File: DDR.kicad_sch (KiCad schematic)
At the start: 1 part, among them U2 rv1126/rv1109

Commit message: PMIC DCDC
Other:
- title: Leaf RV1126 Power -> Leaf RV1126 PMIC RK809
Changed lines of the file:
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@@
   (paper "A4")
   (title_block
-    (title "Leaf RV1126 Power")
+    (title "Leaf RV1126 PMIC RK809")
     (date "2023-02-23")
     (rev "1")

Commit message: updated: PMIC codec
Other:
- title: Leaf RV1126 PMIC RK809 -> Leaf RV1126 PMIC RK809 Codec
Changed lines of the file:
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@@
   (paper "A4")
   (title_block
-    (title "Leaf RV1126 PMIC RK809")
-    (date "2023-02-23")
+    (title "Leaf RV1126 PMIC RK809 Codec")
+    (date "2023-02-25")
     (rev "1")
     (company "Qingdao IotPi Information Technology")

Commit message: updated: titles
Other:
- title: Leaf RV1126 PMIC RK809 Codec -> Leaf RV1126 RK809 DDR
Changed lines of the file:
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@@
   (paper "A4")
   (title_block
-    (title "Leaf RV1126 PMIC RK809 Codec")
+    (title "Leaf RV1126 RK809 DDR")
     (date "2023-02-25")
     (rev "1")

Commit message: updated: DDR
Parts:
- added U4: W634GU6QB, Package_BGA:Micron_FBGA-96_7.5x13.5mm_Layout9x16_P0.8mm, symbol Memory_DDR:W634GU6QB
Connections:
- net DDR resistors/SoC_A8: now reaches U2.A10 (LPDDR4_CLKN_A/DDR4_A10/LPDDR3_A8/DDR3_A8)
- net DDR resistors/SoC_A14: now reaches U2.A11 (LPDDR4_CS1n_B/DDR4_A14_Wen/DDR3_A14)
- net DDR resistors/SoC_A13: now reaches U2.A12 (LPDDR4_A3_A/DDR4_A13/DDR3_A13)
- net DDR resistors/SoC_CKE: now reaches U2.A4 (LPDDR4_A3_B/DDR4_ACTn/LPDDR3_CKE/DDR3_CKE)
- net DDR resistors/SoC_CS0n: now reaches U2.A5 (LPDDR4_A4_B/DDR4_ODT0/LPDDR3_CS0n/DDR3_CS0n)
- net DDR resistors/SoC_WEn: now reaches U2.A6 (LPDDR4_CKE1_B/DDR4_BA1/DDR3_WEn)
- net DDR resistors/SoC_A12: now reaches U2.A7 (LPDDR4_ODT0_B/DDR4_A5/DDR3_A12)
- net DDR resistors/SoC_A1: now reaches U2.A8 (LPDDR4_CKE0_A/DDR4_A8/LPDDR3_A1/DDR3_A1)
- net DDR resistors/SoC_A6: now reaches U2.A9 (LPDDR4_CLKP_A/DDR4_A4/LPDDR3_A6/DDR3_A6)
- net DDR resistors/SoC_A11: now reaches U2.B10 (LPDDR4_CS0n_B/DDR4_A16_RASn/DDR3_A11)
- net DDR resistors/SoC_A9: now reaches U2.B11 (LPDDR4_A4_A/DDR4_A2/LPDDR3_A9/DDR3_A9)
- net DDR resistors/SoC_ODT0: now reaches U2.B4 (LPDDR4_A2_B/DDR4_CS0n/LPDDR3_ODT0/DDR3_ODT0)
- net DDR resistors/SoC_A10: now reaches U2.B5 (LPDDR4_A0_B/DDR4_A15_CASn/DDR3_A10)
- net DDR resistors/SoC_A15: now reaches U2.B6 (LPDDR4_A5_B/DDR4_A3/DDR3_A15)
- net DDR resistors/SoC_BA1: now reaches U2.B7 (LPDDR4_CKE0_B/DDR4_A1/DDR3_BA1)
- net DDR resistors/SoC_A4: now reaches U2.B8 (LPDDR4_ODT0_A/DDR4_A7/LPDDR3_A4/DDR3_A4)
- net DDR resistors/SoC_A5: now reaches U2.B9 (LPDDR4_A5_A/DDR4_A9/LPDDR3_A5/DDR3_A5)
- net DDR resistors/SoC_A7: now reaches U2.C11 (LPDDR4_A2_A/DDR4_A11/LPDDR3_A7/DDR3_A7)
- net DDR resistors/SoC_CASn: now reaches U2.C6 (LPDDR4_A1_B/DDR4_CKE/DDR3_CASn)
- net DDR resistors/SoC_BA2: now reaches U2.C8 (LPDDR4_A0_A/DDR4_A6/DDR3_BA2)
- net DDR resistors/SoC_A3: now reaches U2.C9 (LPDDR4_CKE1_A/DDR4_A0/LPDDR3_A3/DDR3_A3)
- net DDR resistors/SoC_A0: now reaches U2.D10 (LPDDR4_ODT1_B/DDR4_ODT1/LPDDR3_A0/DDR3_A0)
- net DDR resistors/SoC_A2: now reaches U2.D11 (LPDDR4_ODT1_A/DDR4_BG1/LPDDR3_A2/DDR3_A2)
- net DDR resistors/SoC_ODT1: now reaches U2.D6 (LPDDR4_CS1n_A/DDR4_BG0/LPDDR3_ODT1/DDR3_ODT1)
- net DDR resistors/SoC_BA0: now reaches U2.D8 (DDR4_CS1n/DDR3_BA0)
- net DDR resistors/SoC_CS1n: now reaches U2.E7 (LPDDR4_CS0n_A/DDR4_BA0/LPDDR3_CS1n/DDR3_CS1n)
- new net DDR resistors/DDR_A0: U4.N3 (A0)
- new net DDR resistors/DDR_A1: U4.P7 (A1)
- new net DDR resistors/DDR_A10: U4.L7 (A10/AP)
- new net DDR resistors/DDR_A11: U4.R7 (A11)
- new net DDR resistors/DDR_A12: U4.N7 (A12/BC#)
- new net DDR resistors/DDR_A13: U4.T3 (A13)
- new net DDR resistors/DDR_A14: U4.T7 (A14)
- new net DDR resistors/DDR_A2: U4.P3 (A2)
- new net DDR resistors/DDR_A3: U4.N2 (A3)
- new net DDR resistors/DDR_A4: U4.P8 (A4)
- new net DDR resistors/DDR_A5: U4.P2 (A5)
- new net DDR resistors/DDR_A6: U4.R8 (A6)
- new net DDR resistors/DDR_A7: U4.R2 (A7)
- new net DDR resistors/DDR_A8: U4.T8 (A8)
- new net DDR resistors/DDR_A9: U4.R3 (A9)
- new net DDR resistors/DDR_BA0: U4.M2 (BA0)
- new net DDR resistors/DDR_BA1: U4.N8 (BA1)
- new net DDR resistors/DDR_BA2: U4.M3 (BA2)
- new net DDR resistors/DDR_CASn: U4.K3 (CAS#)
- new net DDR resistors/DDR_CKE: U4.K9 (CKE)
- new net DDR resistors/DDR_CS0n: U4.L2 (CS#)
- new net DDR resistors/DDR_ODT0: U4.K1 (ODT)
- new net DDR resistors/DDR_WEn: U4.L3 (WE#)
- no-connect marks 0 -> 3
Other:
- added sheet DDR resistors (DDR_resistors.kicad_sch)
- moved on the sheet: U2N

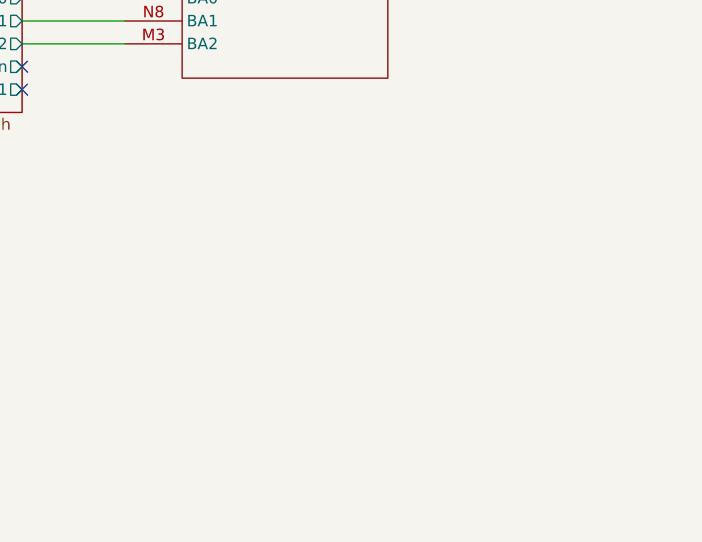
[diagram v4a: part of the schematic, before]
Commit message: added DDR Power
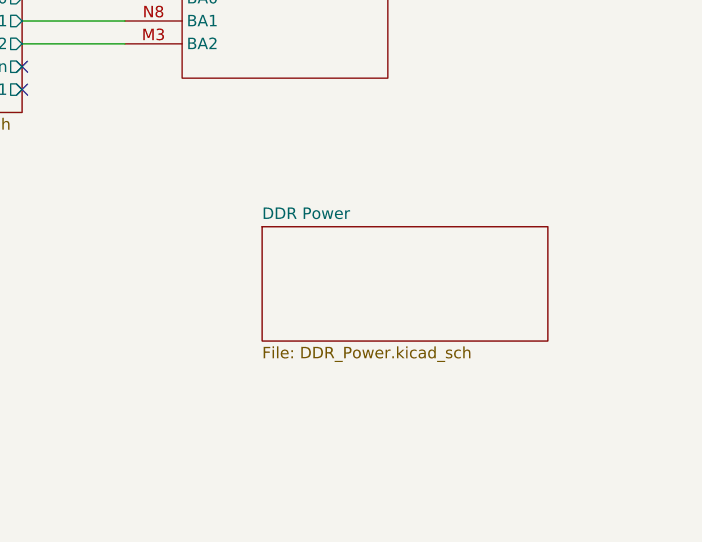
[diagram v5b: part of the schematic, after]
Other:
- added sheet DDR Power (DDR_Power.kicad_sch)
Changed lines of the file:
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@@
+    )
+  )
+  (sheet (at 232.41 127) (size 31.75 12.7) (fields_autoplaced)
+    (stroke (width 0.1524) (type solid))
+    (fill (color 0 0 0 0.0000))
+    (property "Sheetname" "DDR Power" (at 232.41 126.2884 0)
+      (effects (font (size 1.27 1.27)) (justify left bottom))
+    )
+    (property "Sheetfile" "DDR_Power.kicad_sch" (at 232.41 140.2846 0)
+      (effects (font (size 1.27 1.27)) (justify left top))
+    )
+    (instances
+      (project "leaf"
+        (path "/e3b58043-16a3-43c8-9fad-9c9784eebfa4/9453ad46-b3ff-4d4e-8aa6-7cc75aa0f522" (page "18"))
+      )
     )
   )

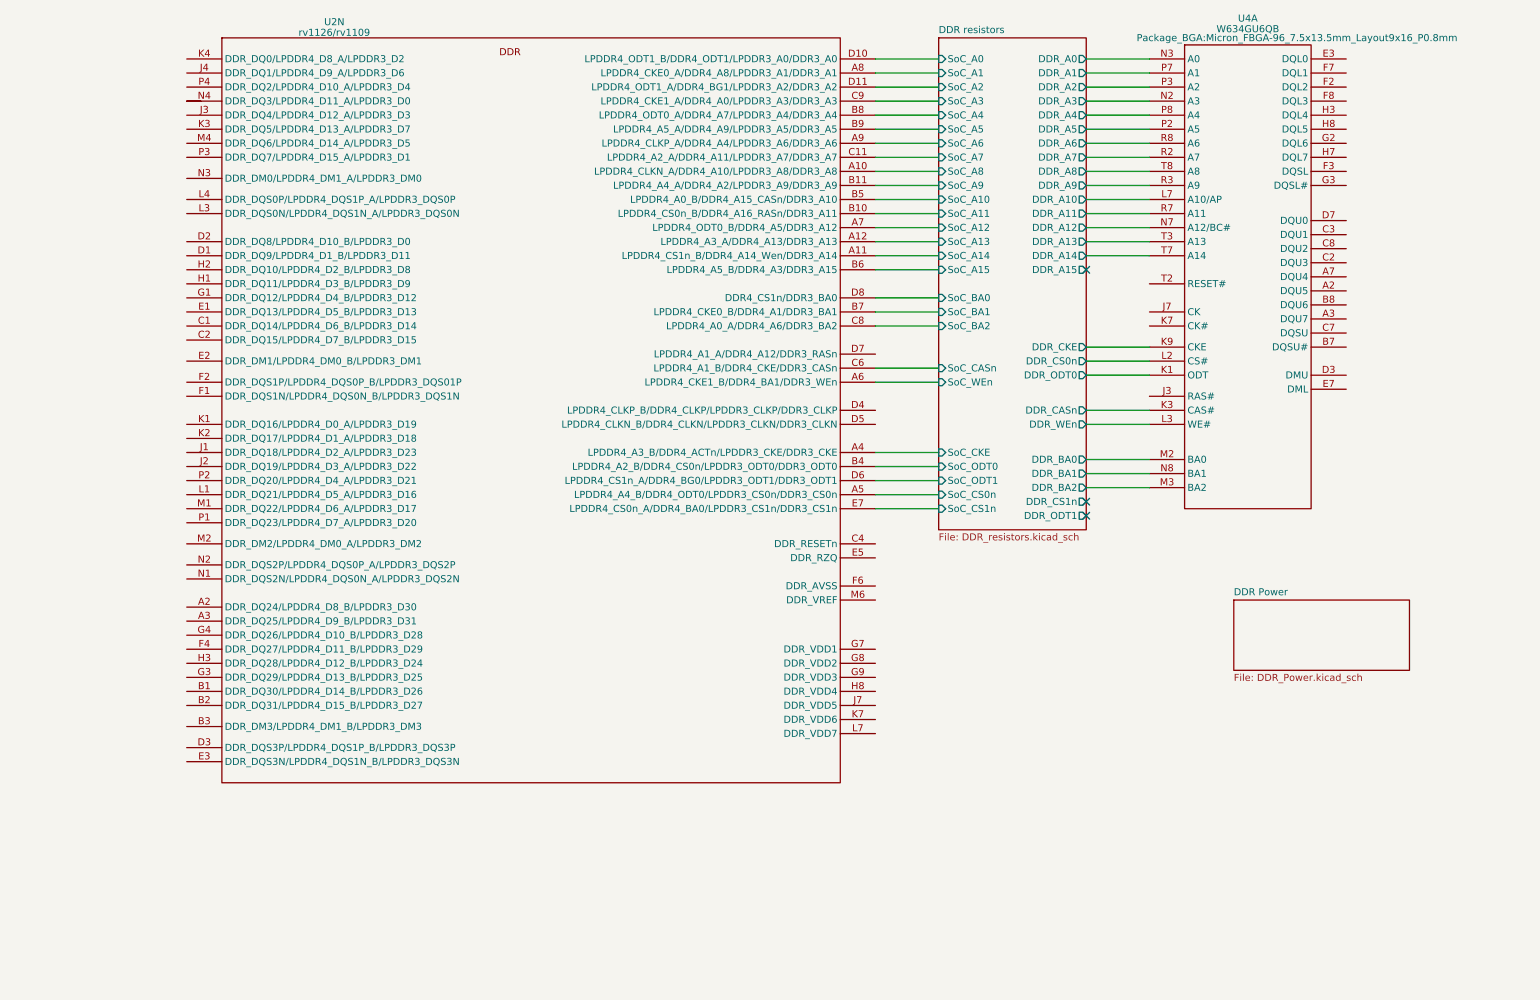
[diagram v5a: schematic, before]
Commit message: updated DDR data lines
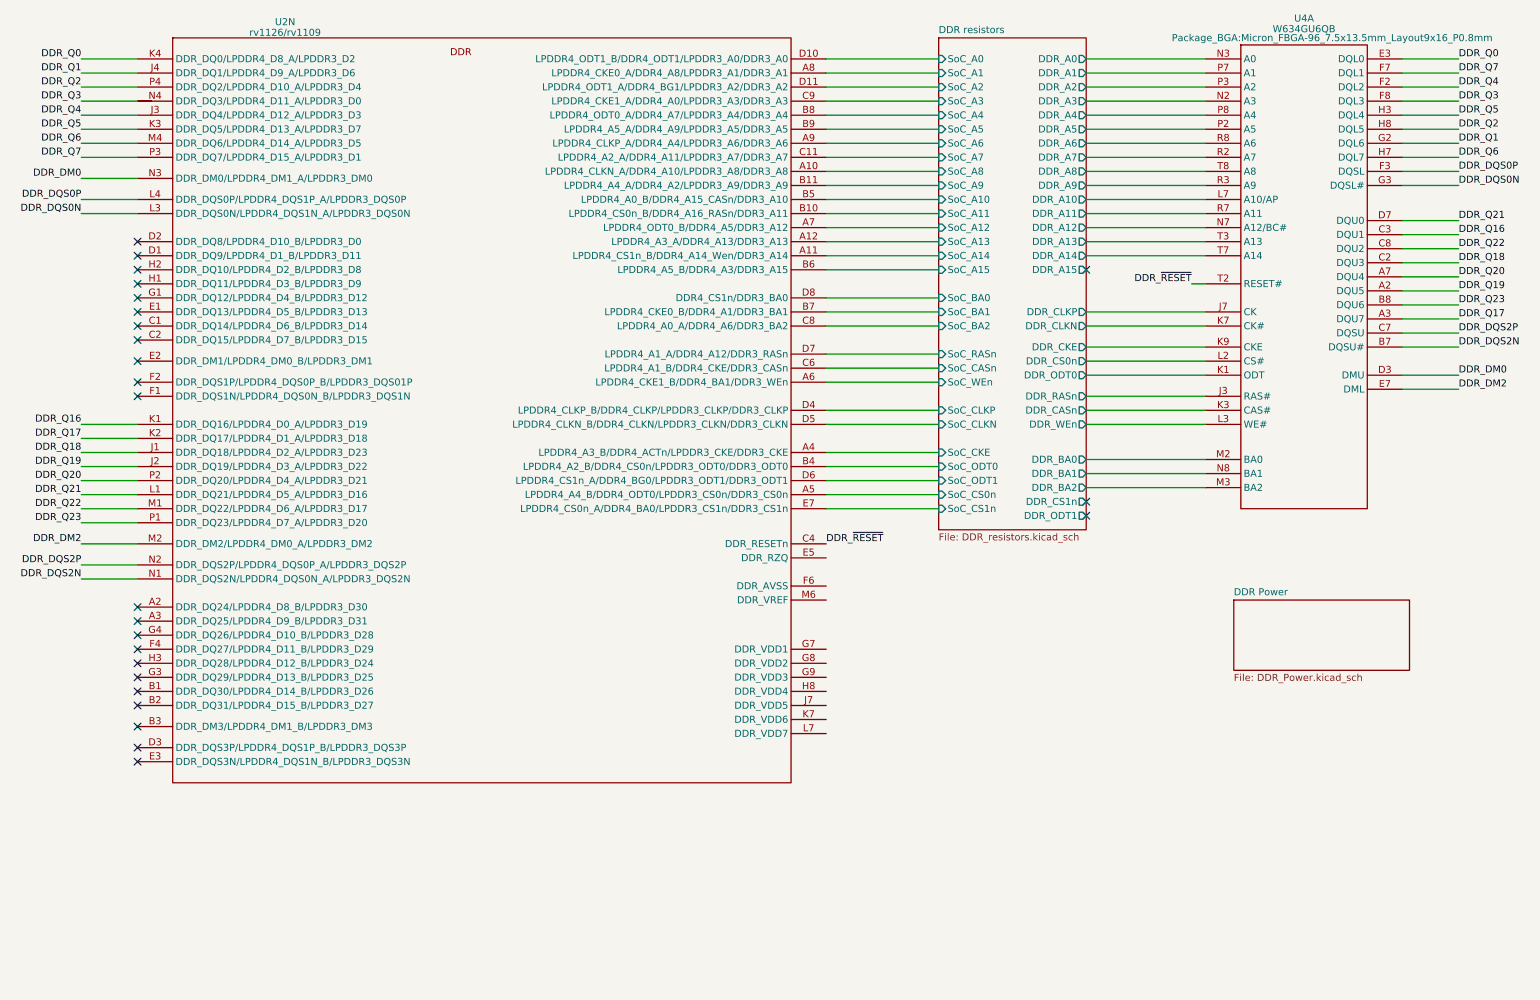
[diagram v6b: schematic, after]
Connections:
- net DDR_Q19: now reaches U4.A2 (DQU5)
- net DDR_Q19: now also U2.J2 (DDR_DQ19/LPDDR4_D3_A/LPDDR3_D22)
- net DDR_Q17: now reaches U4.A3 (DQU7)
- net DDR_Q17: now also U2.K2 (DDR_DQ17/LPDDR4_D1_A/LPDDR3_D18)
- net DDR_Q20: now reaches U4.A7 (DQU4)
- net DDR_Q20: now also U2.P2 (DDR_DQ20/LPDDR4_D4_A/LPDDR3_D21)
- net DDR_DQS2N: now reaches U4.B7 (DQSU#)
- net DDR_DQS2N: now also U2.N1 (DDR_DQS2N/LPDDR4_DQS0N_A/LPDDR3_DQS2N)
- net DDR_Q23: now reaches U4.B8 (DQU6)
- net DDR_Q23: now also U2.P1 (DDR_DQ23/LPDDR4_D7_A/LPDDR3_D20)
- net DDR_Q18: now reaches U4.C2 (DQU3)
- net DDR_Q18: now also U2.J1 (DDR_DQ18/LPDDR4_D2_A/LPDDR3_D23)
- net DDR_Q16: now reaches U4.C3 (DQU1)
- net DDR_Q16: now also U2.K1 (DDR_DQ16/LPDDR4_D0_A/LPDDR3_D19)
- net DDR_DQS2P: now reaches U4.C7 (DQSU)
- net DDR_DQS2P: now also U2.N2 (DDR_DQS2P/LPDDR4_DQS0P_A/LPDDR3_DQS2P)
- net DDR_Q22: now reaches U4.C8 (DQU2)
- net DDR_Q22: now also U2.M1 (DDR_DQ22/LPDDR4_D6_A/LPDDR3_D17)
- net DDR_DM0: now reaches U4.D3 (DMU)
- net DDR_DM0: now also U2.N3 (DDR_DM0/LPDDR4_DM1_A/LPDDR3_DM0)
- net DDR_Q21: now reaches U4.D7 (DQU0)
- net DDR_Q21: now also U2.L1 (DDR_DQ21/LPDDR4_D5_A/LPDDR3_D16)
- net DDR_Q0: now reaches U4.E3 (DQL0)
- net DDR_Q0: now also U2.K4 (DDR_DQ0/LPDDR4_D8_A/LPDDR3_D2)
- net DDR_DM2: now reaches U4.E7 (DML)
- net DDR_DM2: now also U2.M2 (DDR_DM2/LPDDR4_DM0_A/LPDDR3_DM2)
- net DDR_Q4: now reaches U4.F2 (DQL2)
- net DDR_Q4: now also U2.J3 (DDR_DQ4/LPDDR4_D12_A/LPDDR3_D3)
- net DDR_DQS0P: now reaches U4.F3 (DQSL)
- net DDR_DQS0P: now also U2.L4 (DDR_DQS0P/LPDDR4_DQS1P_A/LPDDR3_DQS0P)
- net DDR_Q7: now reaches U4.F7 (DQL1)
- net DDR_Q7: now also U2.P3 (DDR_DQ7/LPDDR4_D15_A/LPDDR3_D1)
- net DDR_Q3: now reaches U4.F8 (DQL3)
- net DDR_Q3: now also U2., U2.N4 (DDR_DQ3/LPDDR4_D11_A/LPDDR3_D0)
- net DDR_Q1: now reaches U4.G2 (DQL6)
- net DDR_Q1: now also U2.J4 (DDR_DQ1/LPDDR4_D9_A/LPDDR3_D6)
- net DDR_DQS0N: now reaches U4.G3 (DQSL#)
- net DDR_DQS0N: now also U2.L3 (DDR_DQS0N/LPDDR4_DQS1N_A/LPDDR3_DQS0N)
- net DDR_Q5: now reaches U4.H3 (DQL4)
- net DDR_Q5: now also U2.K3 (DDR_DQ5/LPDDR4_D13_A/LPDDR3_D7)
- net DDR_Q6: now reaches U4.H7 (DQL7)
- net DDR_Q6: now also U2.M4 (DDR_DQ6/LPDDR4_D14_A/LPDDR3_D5)
- net DDR_Q2: now reaches U4.H8 (DQL5)
- net DDR_Q2: now also U2.P4 (DDR_DQ2/LPDDR4_D10_A/LPDDR3_D4)
- net DDR resistors/DDR_RASn: now reaches U4.J3 (RAS#)
- net DDR resistors/DDR_CLKP: now reaches U4.J7 (CK)
- net DDR resistors/DDR_CLKN: now reaches U4.K7 (CK#)
- net DDR_~{RESET}: now reaches U4.T2 (RESET#)
- net DDR_~{RESET}: now also U2.C4 (DDR_RESETn)
- net DDR resistors/SoC_CLKP: now reaches U2.D4 (LPDDR4_CLKP_B/DDR4_CLKP/LPDDR3_CLKP/DDR3_CLKP)
- net DDR resistors/SoC_CLKN: now reaches U2.D5 (LPDDR4_CLKN_B/DDR4_CLKN/LPDDR3_CLKN/DDR3_CLKN)
- net DDR resistors/SoC_RASn: now reaches U2.D7 (LPDDR4_A1_A/DDR4_A12/DDR3_RASn)
- no-connect marks 3 -> 25
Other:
- sheet DDR resistors ports: added DDR_CLKN, DDR_CLKP, DDR_RASn, SoC_CLKN, SoC_CLKP, SoC_RASn; removed none
- moved on the sheet: U2N, U4A

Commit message: updated DDR
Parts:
- added C57 (x3): 100nF X5R 6.3V, Capacitor_SMD:C_0201_0603Metric, symbol Device:C
- added C57 (x3): 1uF X5R 6.3V, Capacitor_SMD:C_0402_1005Metric, symbol Device:C
- added C57: 10uF X5R 6.3V, Capacitor_SMD:C_0603_1608Metric, symbol Device:C
- added R22: 240R 1%, Resistor_SMD:R_0402_1005Metric, symbol Device:R
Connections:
- net DDR_RZQ: now reaches U2.E5 (DDR_RZQ)
- net DDR_RZQ: now also R22.1
- net VCC_DDR: now reaches U2.G7 (DDR_VDD1)
- net VCC_DDR: now also U2.G8 (DDR_VDD2), U2.G9 (DDR_VDD3), U2.H8 (DDR_VDD4), U2.J7 (DDR_VDD5), U2.K7 (DDR_VDD6), U2.L7 (DDR_VDD7), C57.1, C57.1, C57.1, C57.1, C57.1, C57.1, C57.1
- new net GND: C57.2, C57.2, C57.2, C57.2, C57.2, C57.2, C57.2, R22.2

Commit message: updated Power
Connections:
- net GND: now also U2.F6 (DDR_AVSS)
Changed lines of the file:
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@@
+    (stroke (width 0) (type default))
+  )
+  (wire (pts (xy 158.75 124.46) (xy 168.91 124.46))
     (stroke (width 0) (type default))
   )
@@
         )
       )
+    )
+  )
+  (symbol (lib_id "power:GND") (at 168.91 124.46 90) (unit 1)
+    (in_bom yes) (on_board yes) (dnp no) (fields_autoplaced)
+    (property "Reference" "#PWR057" (at 175.26 124.46 0)
+      (effects (font (size 1.27 1.27)) hide)
+    )
+    (property "Value" "GND" (at 172.085 124.7768 90)
+      (effects (font (size 1.27 1.27)) (justify right))
+    )
+    (property "Footprint" "" (at 168.91 124.46 0)
+      (effects (font (size 1.27 1.27)) hide)
+    )
+    (property "Datasheet" "" (at 168.91 124.46 0)
+      (effects (font (size 1.27 1.27)) hide)
+    )
+    (pin "1")
+    (instances
+      (project "leaf"
+        (path "/e3b58043-16a3-43c8-9fad-9c9784eebfa4/9453ad46-b3ff-4d4e-8aa6-7cc75aa0f522"
+          (reference "#PWR057") (unit 1)
+        )
+      )
